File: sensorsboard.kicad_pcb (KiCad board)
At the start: 2 copper layers, 56.6 x 58.9 mm, 45 parts, among them J1 Conn_01x05_Female, J2 USB_B_Micro, J3 Conn_01x03_Female, J4 SWD, J5 Conn_01x02_Male, J6 Conn_01x03_Male, J7 USB_B_Micro, J8 Conn_02x05_Odd_Even, J9 UART, SW1 nRF_Reset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

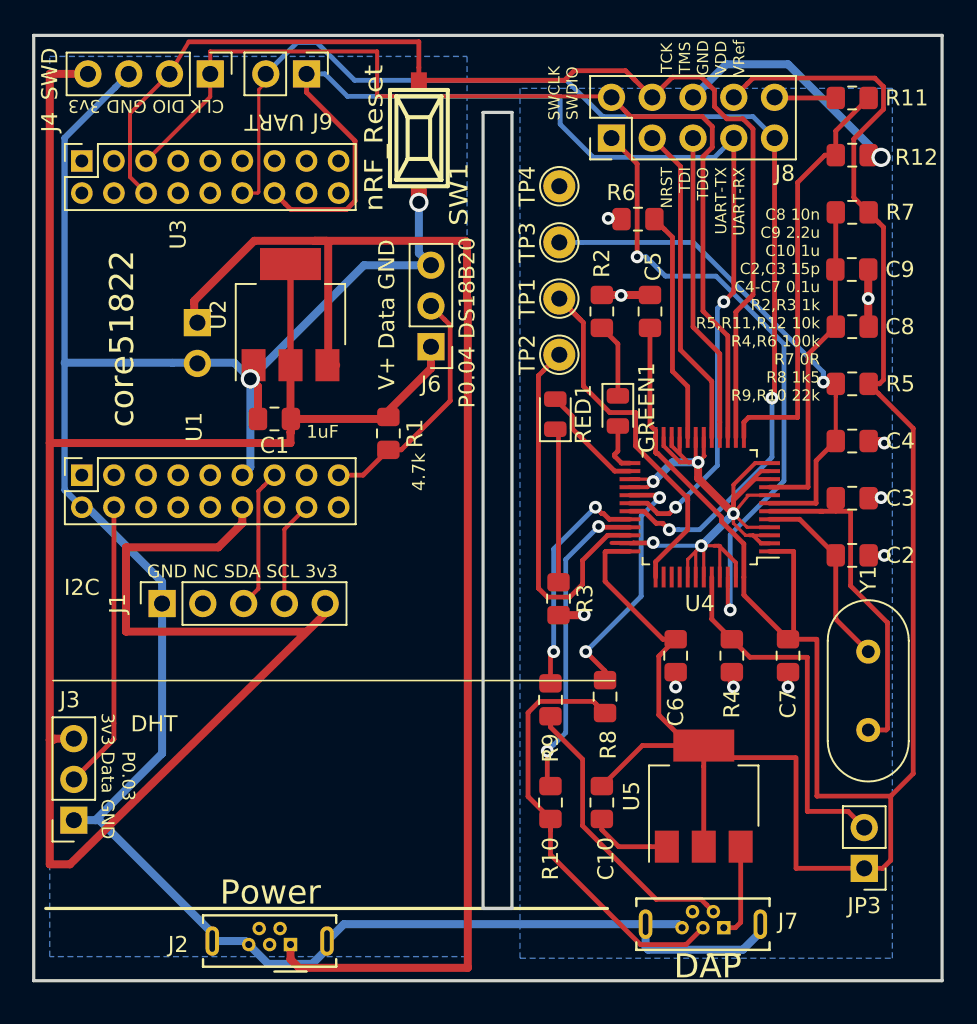
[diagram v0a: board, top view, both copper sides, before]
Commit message: Fix AMS1117 GND connection
Signed-off-by: Zamir SUN <sztsian@gmail.com>
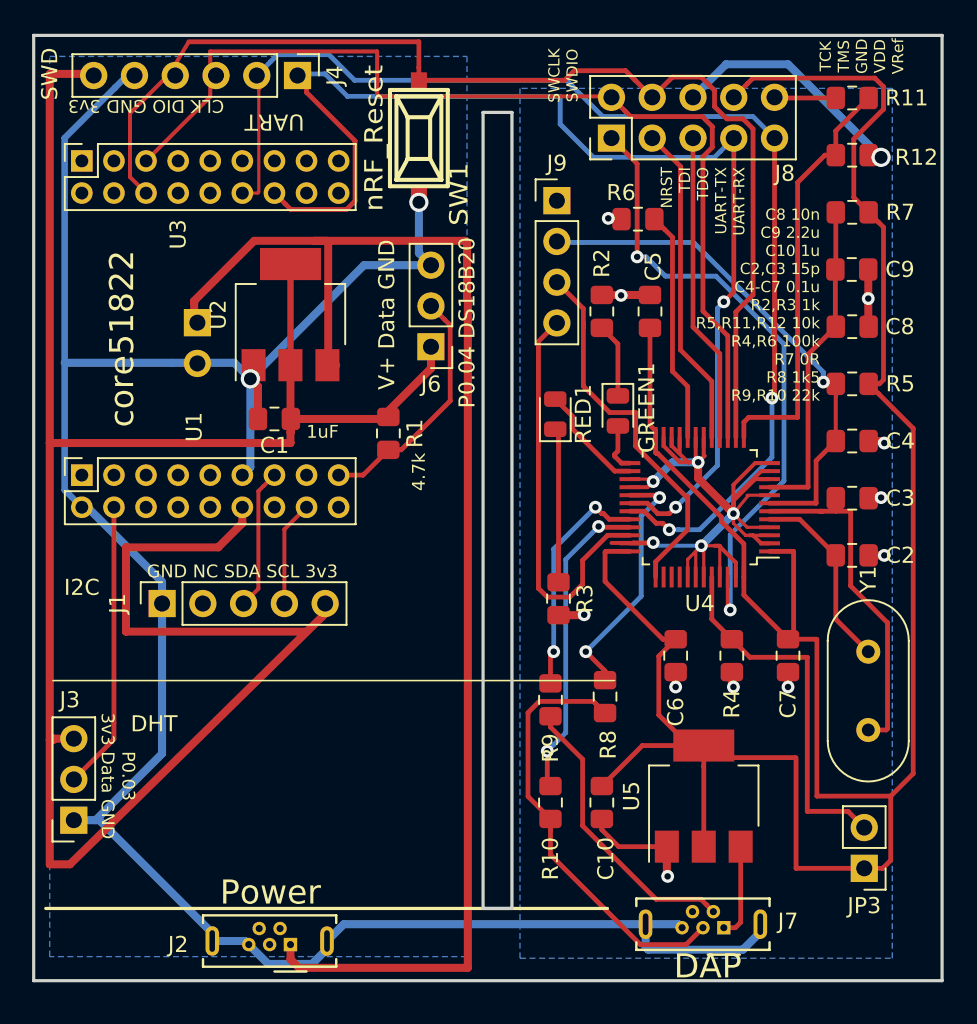
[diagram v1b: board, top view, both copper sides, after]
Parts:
- removed TP1: SWCLK_SELF, TestPoint:TestPoint_THTPad_D2.0mm_Drill1.0mm
- removed TP2: SWDIO_SELF, TestPoint:TestPoint_THTPad_D2.0mm_Drill1.0mm
- removed TP3: NRST, TestPoint:TestPoint_THTPad_D2.0mm_Drill1.0mm
- removed TP4: TestPoint, TestPoint:TestPoint_THTPad_D2.0mm_Drill1.0mm
- J4: value SWD -> Conn_01x06_Male; footprint Connector_PinHeader_2.54mm:PinHeader_1x04_P2.54mm_Vertical -> Connector_PinHeader_2.54mm:PinHeader_1x06_P2.54mm_Vertical
- J9: value UART -> Self_Flash; footprint Connector_PinHeader_2.54mm:PinHeader_1x02_P2.54mm_Vertical -> Connector_PinHeader_2.54mm:PinHeader_1x04_P2.54mm_Vertical
- moved J9 17.5 mm to (124.6, 95.9), turned to 0 degrees
- moved J4 5.44 mm to (108.4, 88.1)
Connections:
- C10 pad 2: Net-(C10-Pad2) -> GND
- J4 pad 1: PA5-SWCLK-TCK -> PA9-TX
- J4 pad 2: PA4-SWDIO-TMS -> PA10-RX
- J4 pad 3: GND -> PA5-SWCLK-TCK
- J4 pad 4: +3V3 -> PA4-SWDIO-TMS
- J9 pad 1: PA9-TX -> GND
- J9 pad 2: PA10-RX -> RESET1-TP3
- U5 pad 1: Net-(C10-Pad2) -> GND
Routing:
- net GND: track 241.3 -> 248.3 mm, vias 18 -> 19
- net Net-(C10-Pad2): track 5.16 -> 0.00 mm
- net PA13-SWDIO: track 23.5 -> 25.4 mm
- net PA14-SWCLK: track 24.6 -> 24.1 mm

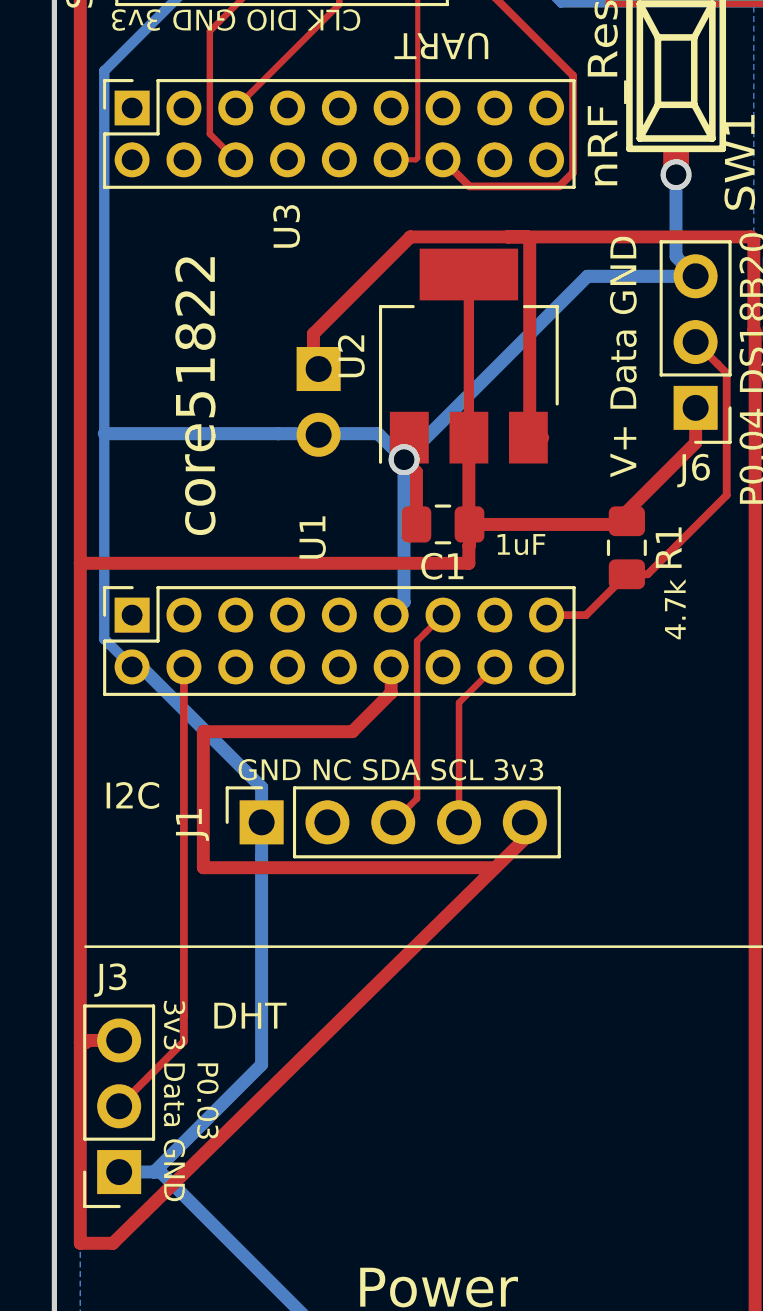
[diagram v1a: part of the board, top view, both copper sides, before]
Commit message: Fix RX/TX connection to core51822
Signed-off-by: Zamir SUN <sztsian@gmail.com>
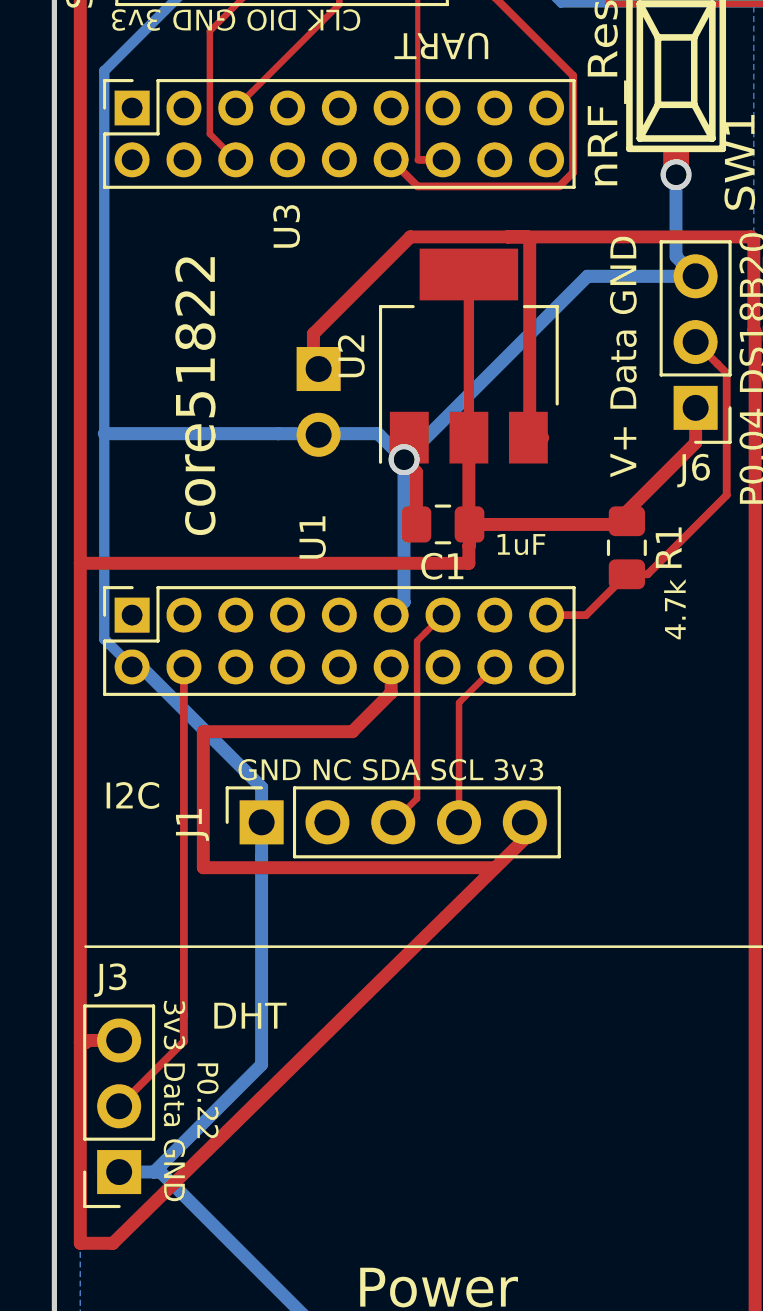
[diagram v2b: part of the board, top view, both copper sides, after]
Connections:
- U3 pad 12: PA10-RX -> PA9-TX
- U3 pad 14: PA9-TX -> PA10-RX
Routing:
- net PA9-TX: track 72.9 -> 74.9 mm
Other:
- board text added: "P0.22 3v3 Data GND"
- board text removed: "P0.03 3v3 Data GND"
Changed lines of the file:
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@@
     (thickness 1.6)
     (drawings 31)
-    (tracks 527)
+    (tracks 525)
     (zones 0)
     (modules 41)
@@
       (net 18 "Net-(U3-Pad15)"))
     (pad 14 thru_hole oval (at -2 12 90) (size 1.35 1.35) (drill 0.8) (layers *.Cu *.Mask)
-      (net 49 PA9-TX))
+      (net 50 PA10-RX))
     (pad 13 thru_hole oval (at 0 12 90) (size 1.35 1.35) (drill 0.8) (layers *.Cu *.Mask)
       (net 19 "Net-(U3-Pad13)"))
     (pad 12 thru_hole oval (at -2 10 90) (size 1.35 1.35) (drill 0.8) (layers *.Cu *.Mask)
-      (net 50 PA10-RX))
+      (net 49 PA9-TX))
     (pad 11 thru_hole oval (at 0 10 90) (size 1.35 1.35) (drill 0.8) (layers *.Cu *.Mask)
       (net 20 "Net-(U3-Pad11)"))
@@
     (effects (font (size 1 1) (thickness 0.25)))
   )
-  (gr_text "P0.03\n3v3 Data GND" (at 97.25 131.75 270) (layer F.SilkS)
+  (gr_text "P0.22\n3v3 Data GND" (at 97.25 131.75 270) (layer F.SilkS)
     (effects (font (size 0.8 0.8) (thickness 0.2)))
   )
@@
   (segment (start 134.6 112.4) (end 134.600001 102.599999) (width 0.3) (layer B.Cu) (net 49))
   (segment (start 132 115) (end 134.6 112.4) (width 0.3) (layer B.Cu) (net 49))
-  (segment (start 107.674999 96.099998) (end 107 95.424999) (width 0.3) (layer F.Cu) (net 49))
-  (segment (start 108.025001 96.45) (end 107.674999 96.099998) (width 0.3) (layer F.Cu) (net 49))
-  (segment (start 111.492001 96.45) (end 108.025001 96.45) (width 0.3) (layer F.Cu) (net 49))
-  (segment (start 112.025001 95.917) (end 111.492001 96.45) (width 0.3) (layer F.Cu) (net 49))
-  (segment (start 112.025001 92.175001) (end 112.025001 95.917) (width 0.3) (layer F.Cu) (net 49))
-  (segment (start 109 89.15) (end 112.025001 92.175001) (width 0.3) (layer F.Cu) (net 49))
-  (segment (start 109 88) (end 109 89.15) (width 0.3) (layer F.Cu) (net 49))
   (segment (start 110.15 88) (end 111.55 89.4) (width 0.3) (layer B.Cu) (net 49))
   (segment (start 109 88) (end 110.15 88) (width 0.3) (layer B.Cu) (net 49))
@@
   (segment (start 134.770001 92.849999) (end 135.62 92) (width 0.3) (layer B.Cu) (net 49))
   (segment (start 124.8 89.4) (end 124.8 91.130002) (width 0.3) (layer B.Cu) (net 49))
+  (segment (start 111.492001 96.45) (end 106.025001 96.45) (width 0.3) (layer F.Cu) (net 49))
+  (segment (start 112.025001 95.917) (end 111.492001 96.45) (width 0.3) (layer F.Cu) (net 49))
+  (segment (start 112.025001 92.175001) (end 112.025001 95.917) (width 0.3) (layer F.Cu) (net 49))
+  (segment (start 106.025001 96.45) (end 105 95.424999) (width 0.3) (layer F.Cu) (net 49))
+  (segment (start 109 88) (end 109 89.15) (width 0.3) (layer F.Cu) (net 49))
+  (segment (start 109 89.15) (end 112.025001 92.175001) (width 0.3) (layer F.Cu) (net 49))
   (via (at 131.6 116.4) (size 0.8) (drill 0.4) (layers F.Cu B.Cu) (net 50))
   (via (at 138 108.2) (size 0.8) (drill 0.4) (layers F.Cu B.Cu) (net 50))
@@
   (segment (start 138 108.2) (end 138 111.889998) (width 0.3) (layer B.Cu) (net 50))
   (segment (start 106.024999 95.354594) (end 106.024999 88.975001) (width 0.2) (layer F.Cu) (net 50))
-  (segment (start 105 95.424999) (end 105.954594 95.424999) (width 0.2) (layer F.Cu) (net 50))
-  (segment (start 105.954594 95.424999) (end 106.024999 95.354594) (width 0.2) (layer F.Cu) (net 50))
   (segment (start 106.46 88.54) (end 106.46 88) (width 0.2) (layer F.Cu) (net 50))
   (segment (start 106.024999 88.975001) (end 106.46 88.54) (width 0.2) (layer F.Cu) (net 50))
@@
   (segment (start 127.460001 90.660001) (end 125.2 88.4) (width 0.3) (layer B.Cu) (net 50))
   (segment (start 125.2 88.4) (end 112 88.4) (width 0.3) (layer B.Cu) (net 50))
-  (segment (start 106.749999 87.250001) (end 105.9 88.1) (width 0.3) (layer B.Cu) (net 50))
-  (segment (start 107.2 86.8) (end 106.749999 87.250001) (width 0.3) (layer B.Cu) (net 50))
   (segment (start 110.4 86.8) (end 107.2 86.8) (width 0.3) (layer B.Cu) (net 50))
   (segment (start 112 88.4) (end 110.4 86.8) (width 0.3) (layer B.Cu) (net 50))
+  (segment (start 107.2 86.8) (end 106.749999 87.250001) (width 0.3) (layer B.Cu) (net 50))
+  (segment (start 106.749999 87.250001) (end 105.9 88.1) (width 0.3) (layer B.Cu) (net 50))
+  (segment (start 106.045406 95.424999) (end 107 95.424999) (width 0.3) (layer F.Cu) (net 50))
   (segment (start 138.2 89.5) (end 138.16 89.46) (width 0.3) (layer F.Cu) (net 51))
   (segment (start 141.975 89.5) (end 138.2 89.5) (width 0.3) (layer F.Cu) (net 51))
